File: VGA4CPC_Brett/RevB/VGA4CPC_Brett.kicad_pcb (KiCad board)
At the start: 2 copper layers, 78.7 x 106 mm, 45 parts, among them J1 +5V IN, J2 CPC PLUS AUDIO OUT, J3 CPC PLUS VIDEO IN, J4 CPC VIDEO IN, J5 VFREQ, J6 VGA OUT, J7 LUM OUT, SW1 RESET, U1 TLV3202AID, U2 TLV3202AID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

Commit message: Added BOM to schematic
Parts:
- renumbered U3 to U1, U5 to U2, U1 to U3, U2 to U4, U4 to U5
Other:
- board text added: "NOT YET TESTED"

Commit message: Silkscreen updates
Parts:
- U3, U4, U5: value TLV3202AID -> TLV3202
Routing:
- net /200mV: track 57.5 -> 84.3 mm
- net GND: track 452.5 -> 436.8 mm
- net /600mV: track 51.7 -> 53.1 mm, vias 3 -> 0
- net /LUM: track 139.2 -> 138.4 mm
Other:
- board text added: "+3.3V OUT"
- board text added: "+5V IN"
- board text added: "200mV"
- board text added: "600mV"
- board text added: "BLUE"
- board text added: "BUFFER IN"
- board text added: "BUFFER OUT"
- board text added: "B_{0}"
- board text added: "B_{1}"
- board text added: "CSYNC"
- board text added: "GND"
- board text added: "GREEN"
- board text added: "G_{0}"
- board text added: "G_{1}"
- board text added: "INT_VSYNC"
- board text added: "LEFT"
- board text added: "LUM"
- board text added: "RED"
- board text added: "RESET"
- board text added: "RIGHT"
- board text added: "R_{0}"
- board text added: "R_{1}"
- board text added: "VGA_B_{1}"
- board text added: "VGA_B_{2}"
- board text added: "VGA_G_{1}"
- board text added: "VGA_G_{2}"
- board text added: "VGA_HSYNC"
- board text added: "VGA_R_{1}"
- board text added: "VGA_R_{2}"
- board text added: "VGA_VSYNC"
- board text added: "VREQ"

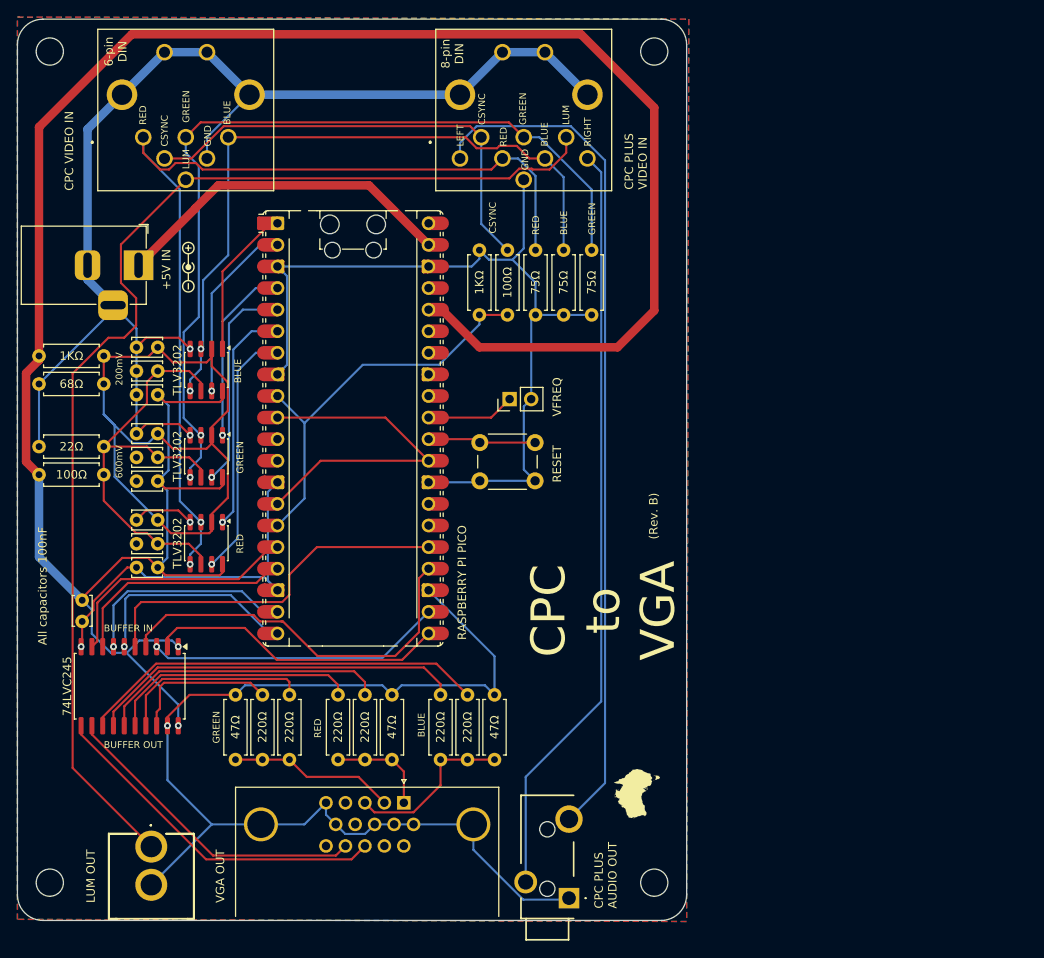
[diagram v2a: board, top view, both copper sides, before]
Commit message: Spare GPIO ports routed
[1] Additional WACKED button (GPIO 21) for "future use"
[2] Spare GPIO 8/9/20 brought out to pin header for "future use"
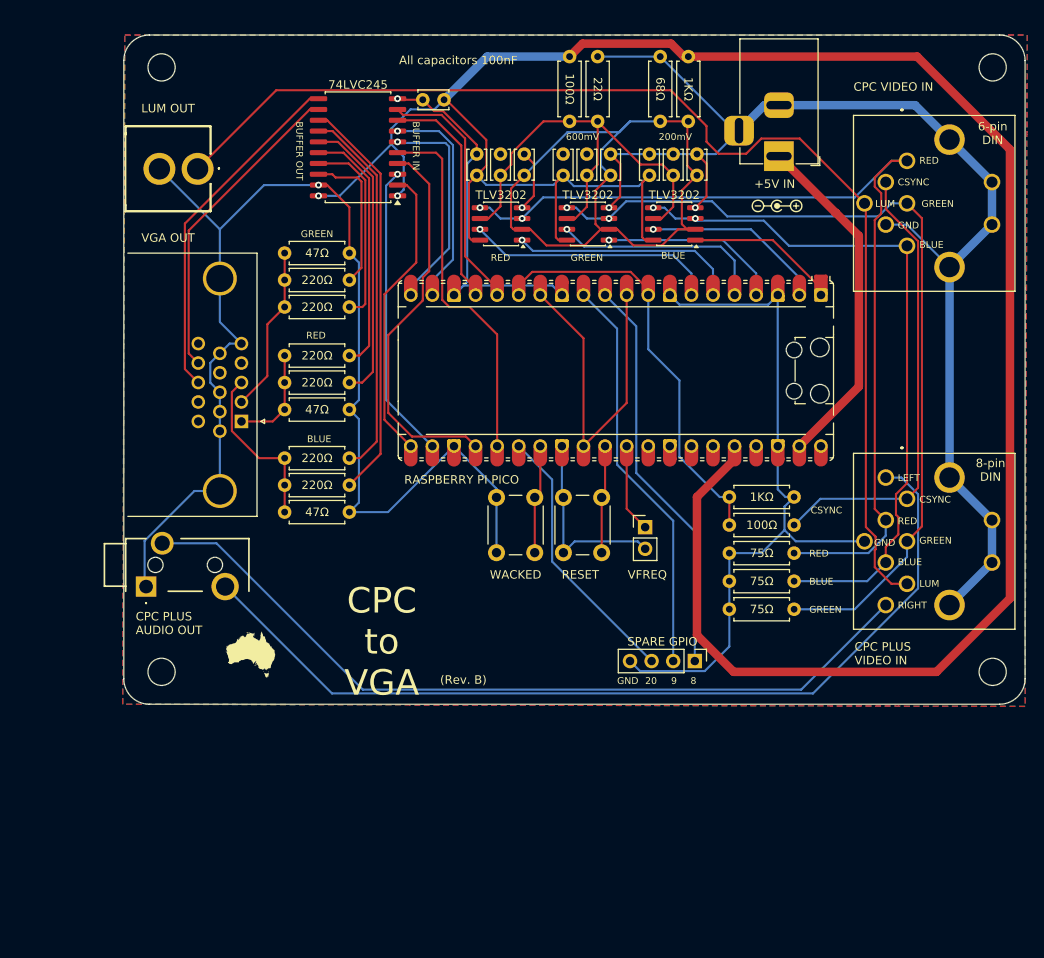
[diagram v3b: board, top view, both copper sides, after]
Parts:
- added J8: SPARE GPIO, Connector_PinHeader_2.54mm:PinHeader_1x04_P2.54mm_Vertical, F.Cu at (149.5, 121.2)
- added SW2: WACKED, Button_Switch_THT:SW_PUSH_6mm, F.Cu at (130.7, 102.0)
- moved H2 111.0 mm to (184.6, 51.4), turned to -90 degrees
- moved H3 96.8 mm to (86.8, 51.4), turned to -90 degrees
- moved J4 89.9 mm to (174.5, 62.4), turned to 90 degrees
- moved R1 84.1 mm to (148.8, 50.1), turned to -90 degrees
- moved H1 83.1 mm to (184.6, 122.5), turned to -90 degrees
- moved J7 79.9 mm to (91.1, 63.3), turned to -90 degrees
- moved R2 79.5 mm to (134.8, 50.1), turned to -90 degrees
- moved J1 76.4 mm to (159.5, 61.8), turned to -90 degrees
- moved C10 73.3 mm to (117.5, 55.2), turned to 0 degrees
- moved R3 72.4 mm to (145.5, 57.7), turned to 90 degrees
- moved R4 69.6 mm to (138.1, 57.7), turned to 90 degrees
- moved U2 68.9 mm to (109.9, 60.8), turned to 180 degrees
- moved C2 66.6 mm to (149.8, 64.1), turned to 90 degrees
- moved J3 65.7 mm to (174.5, 102.2), turned to 90 degrees
- moved C3 64.9 mm to (147.0, 64.1), turned to 90 degrees
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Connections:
- U1 pad 11: unconnected-(U1-GPIO8-Pad11) -> /GPIO8
- U1 pad 12: unconnected-(U1-GPIO9-Pad12)_1 -> /GPIO9
- U1 pad 26: unconnected-(U1-GPIO20-Pad26)_1 -> /GPIO20
- U1 pad 27: unconnected-(U1-GPIO21-Pad27)_1 -> Net-(U1-GPIO21)
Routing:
- net /GPIO9: track 0.00 -> 47.4 mm
- net /GPIO8: track 0.00 -> 47.4 mm
- net /GPIO20: track 0.00 -> 31.8 mm
- net GND: track 436.8 -> 459.7 mm
- net Net-(U1-GPIO21): track 0.00 -> 12.0 mm
- net /CPC_AUDIO_R: track 89.5 -> 96.4 mm
- net /CPC_AUDIO_L: track 100.6 -> 107.5 mm
- net /CSYNC: track 48.4 -> 50.9 mm
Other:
- board size 78.7 x 106 mm -> 106 x 78.7 mm
- board text added: "20"
- board text added: "8"
- board text added: "9"

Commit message: Broke out extra spare GPIO ports
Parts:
- J8: footprint Connector_PinHeader_2.54mm:PinHeader_1x04_P2.54mm_Vertical -> Connector_PinHeader_2.54mm:PinHeader_1x06_P2.54mm_Vertical
- U3, U4, U5: value TLV3202 -> TLV3212
- moved J8 1.39 mm to (150.9, 121.7)
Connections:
- J8 pad 1: /GPIO8 -> /GPIO28
- J8 pad 2: /GPIO9 -> /GPIO27
- J8 pad 3: /GPIO20 -> /GPIO8
- J8 pad 4: GND -> /GPIO9
- U1 pad 32: unconnected-(U1-GPIO27_ADC1-Pad32) -> /GPIO27
- U1 pad 34: unconnected-(U1-GPIO28_ADC2-Pad34)_1 -> /GPIO28
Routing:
- net /GPIO27: track 0.00 -> 27.5 mm
- net /GPIO28: track 0.00 -> 26.4 mm
- net /LUM: track 138.4 -> 143.8 mm
- net +3.3V: track 282.2 -> 279.5 mm
- net /GPIO9: track 47.4 -> 48.6 mm
- net GND: track 459.7 -> 460.9 mm
- net /GPIO20: track 31.8 -> 30.6 mm
- net /GPIO8: track 47.4 -> 48.0 mm
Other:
- board text added: "27"
- board text added: "28"
